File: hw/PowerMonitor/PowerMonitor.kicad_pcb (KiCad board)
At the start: 2 copper layers, 100 x 100 mm, 108 parts, among them J1 Conn_01x02_Socket, J2 Conn_01x02_Socket, J3 Conn_01x02_Socket, J4 Conn_01x02_Socket, J5 Conn_01x02_Socket, Q1 Q_PMOS_GDS, Q2 Q_PMOS_GDS, Q3 Q_PMOS_GDS, U1 TPS54202DDC, U10 LM358, U11 LM393, U12 74LVC1G32, U13 LM358, U14 LM393, U15 74LVC1G32, U2 74LVC1G32, U3 74LVC1G32, U4 NE555D, U5 LM358, U6 LM358, U7 LM358, U8 LM393, U9 74LVC1G32

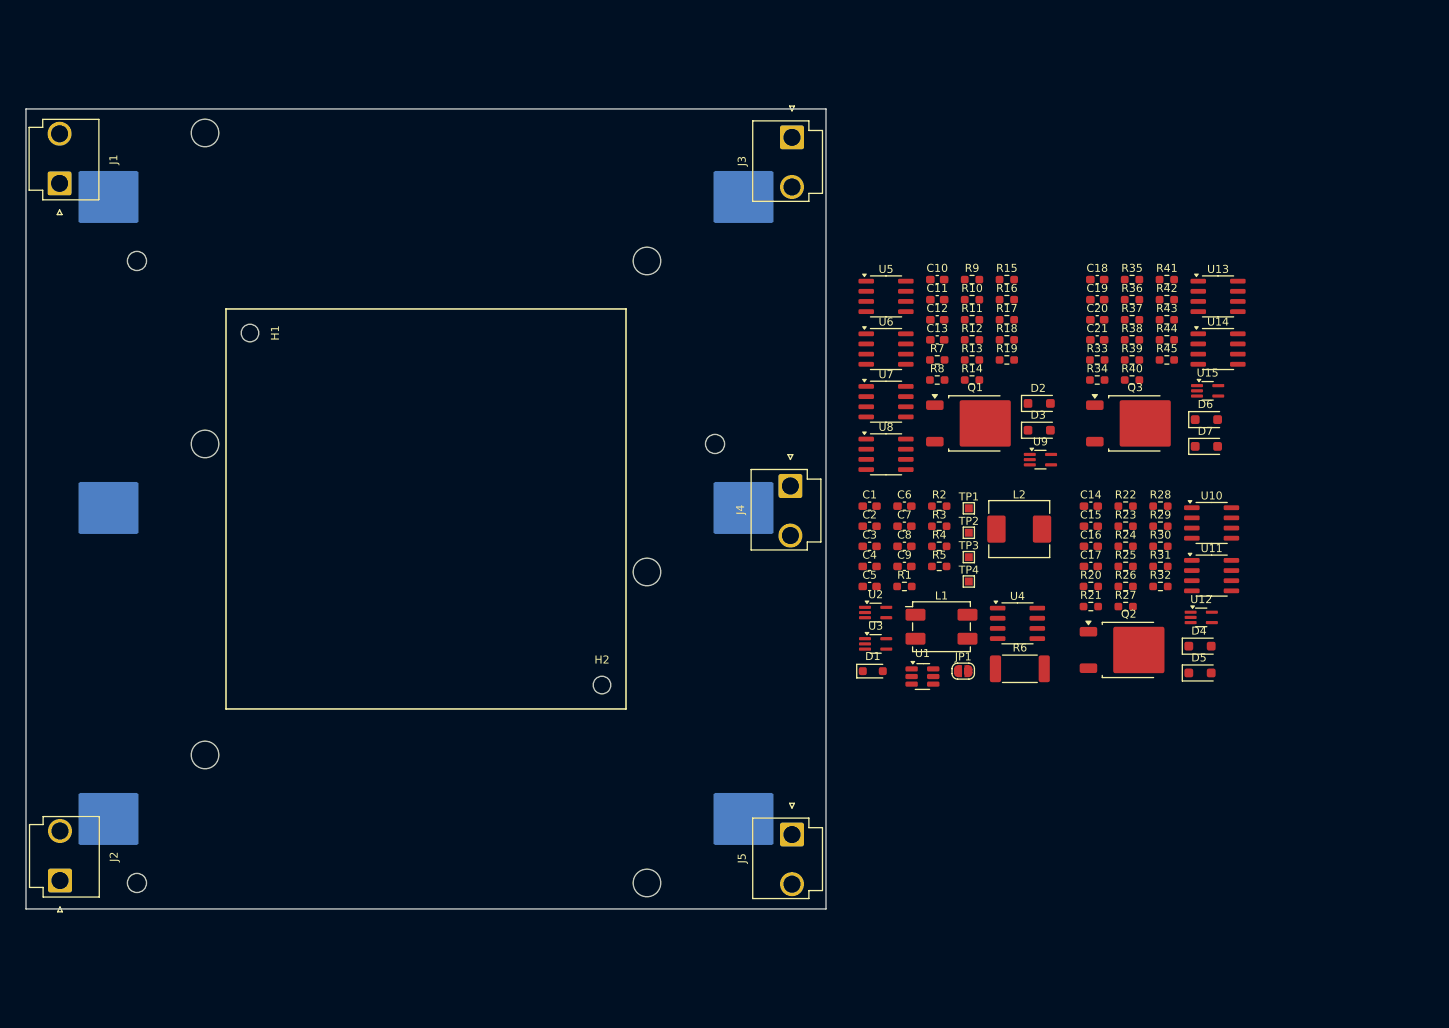
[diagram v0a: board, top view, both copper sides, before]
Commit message: ad uvov in powermon, overcurrent and prepare for latch alarm
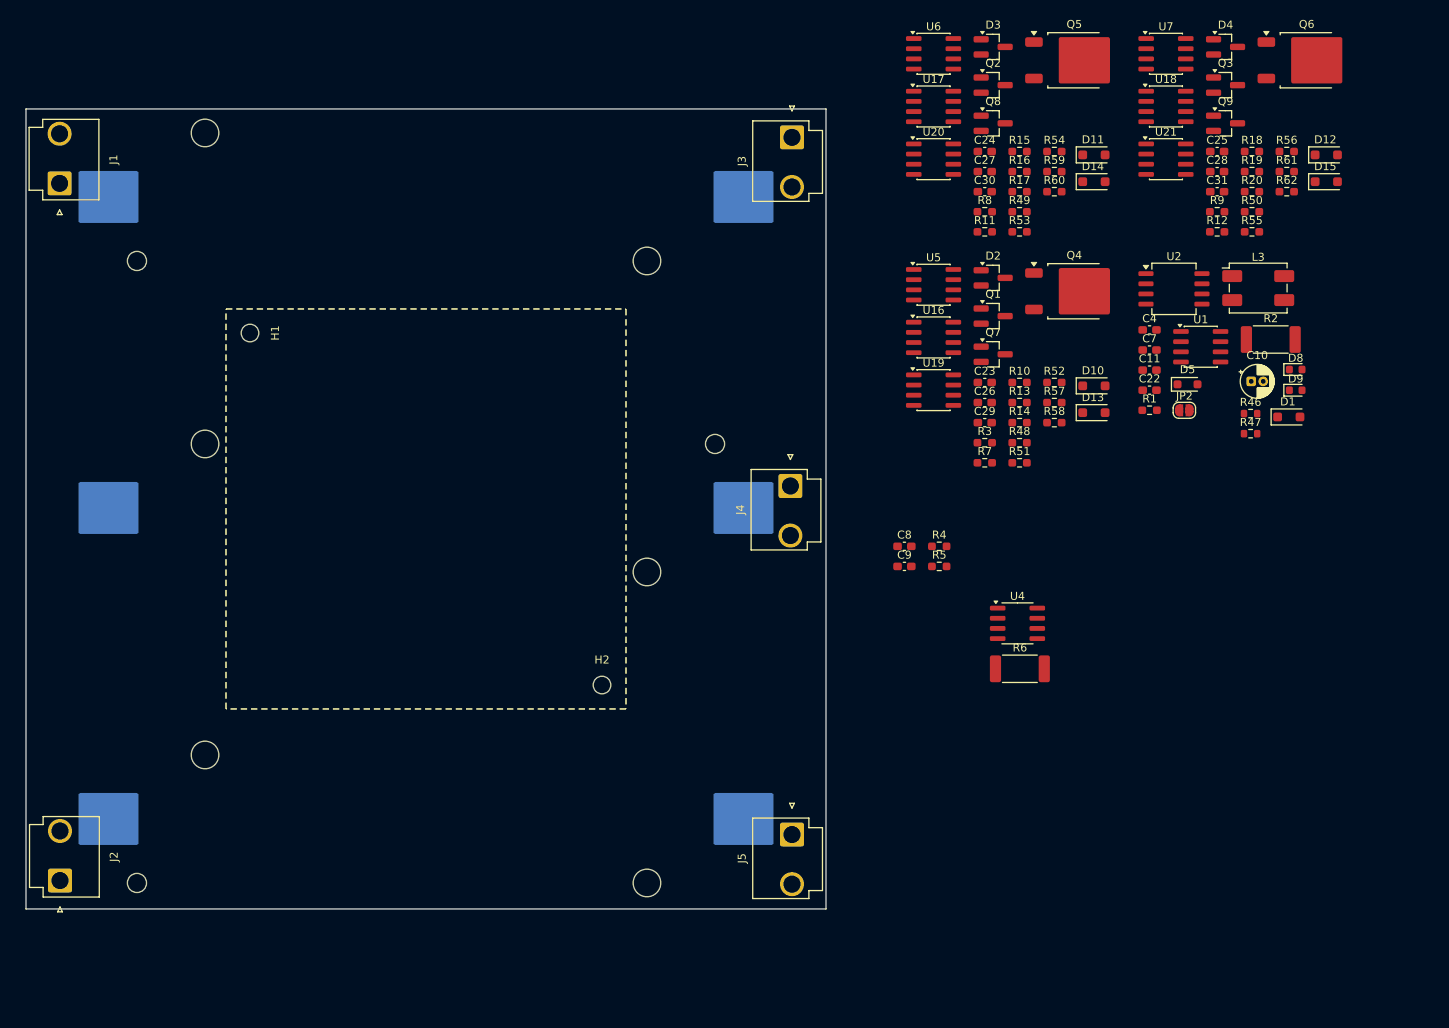
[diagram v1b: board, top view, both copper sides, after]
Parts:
- removed C1: 10 µF, Capacitor_SMD:C_0603_1608Metric_Pad1.08x0.95mm_HandSolder
- removed C12, C13, C15, C16, C17, C19, C20, C21: 1u, Capacitor_SMD:C_0603_1608Metric_Pad1.08x0.95mm_HandSolder
- removed C14, C18: 33n, Capacitor_SMD:C_0603_1608Metric_Pad1.08x0.95mm_HandSolder
- removed C2, C3: 0.1 µF, Capacitor_SMD:C_0603_1608Metric_Pad1.08x0.95mm_HandSolder
- removed C5, C6: 22 µF, Capacitor_SMD:C_0603_1608Metric_Pad1.08x0.95mm_HandSolder
- removed D6, D7: BZT52Bxx, Diode_SMD:D_SOD-123F
- removed JP1: SolderJumper_2_Open, Jumper:SolderJumper-2_P1.3mm_Open_RoundedPad1.0x1.5mm
- removed L1: L_Ferrite_Coupled_1423, Inductor_SMD:L_CommonModeChoke_TDK_ACM7060
- removed L2: KOHER_MDA7030 15uH, Inductor_SMD:L_KOHERelec_MDA7030
- removed R21, R22, R23, R24, R33, R34, R35, R36, R37: 1k, Resistor_SMD:R_0603_1608Metric_Pad0.98x0.95mm_HandSolder
- removed R25, R38: 5.6k, Resistor_SMD:R_0603_1608Metric_Pad0.98x0.95mm_HandSolder
- removed R26, R39: 1.8k, Resistor_SMD:R_0603_1608Metric_Pad0.98x0.95mm_HandSolder
- removed R27, R28, R40, R41: 150, Resistor_SMD:R_0603_1608Metric_Pad0.98x0.95mm_HandSolder
- removed R29, R42: 16k, Resistor_SMD:R_0603_1608Metric_Pad0.98x0.95mm_HandSolder
- removed R30, R43: 2k, Resistor_SMD:R_0603_1608Metric_Pad0.98x0.95mm_HandSolder
- removed R31, R32, R44, R45: 4.7k, Resistor_SMD:R_0603_1608Metric_Pad0.98x0.95mm_HandSolder
- removed TP1, TP2, TP3, TP4: TestPoint_Flag, TestPoint:TestPoint_Pad_1.0x1.0mm
- removed U10, U13: LM358, Package_SO:SOIC-8_3.9x4.9mm_P1.27mm
- removed U11, U14, U8: LM393, Package_SO:SOIC-8_3.9x4.9mm_P1.27mm
- removed U12, U15, U3, U9: 74LVC1G32, Package_TO_SOT_SMD:SOT-353_SC-70-5_Handsoldering
- added C22: 0.01 µF, Capacitor_SMD:C_0603_1608Metric_Pad1.08x0.95mm_HandSolder, F.Cu at (236.2, 75.7)
- added C23: 33n, Capacitor_SMD:C_0603_1608Metric_Pad1.08x0.95mm_HandSolder, F.Cu at (215.6, 74.7)
- added C24: 33n, Capacitor_SMD:C_0603_1608Metric_Pad1.08x0.95mm_HandSolder, F.Cu at (215.6, 45.8)
- added C25: 33n, Capacitor_SMD:C_0603_1608Metric_Pad1.08x0.95mm_HandSolder, F.Cu at (244.6, 45.8)
- added C26: 1u, Capacitor_SMD:C_0603_1608Metric_Pad1.08x0.95mm_HandSolder, F.Cu at (215.6, 77.2)
- added C27: 1u, Capacitor_SMD:C_0603_1608Metric_Pad1.08x0.95mm_HandSolder, F.Cu at (215.6, 48.3)
- added C28: 1u, Capacitor_SMD:C_0603_1608Metric_Pad1.08x0.95mm_HandSolder, F.Cu at (244.6, 48.3)
- added C29: 1u, Capacitor_SMD:C_0603_1608Metric_Pad1.08x0.95mm_HandSolder, F.Cu at (215.6, 79.7)
- added C30: 1u, Capacitor_SMD:C_0603_1608Metric_Pad1.08x0.95mm_HandSolder, F.Cu at (215.6, 50.8)
- added C31: 1u, Capacitor_SMD:C_0603_1608Metric_Pad1.08x0.95mm_HandSolder, F.Cu at (244.6, 50.8)
- added D10: BZT52Bxx, Diode_SMD:D_SOD-123F, F.Cu at (229.2, 75.1)
- added D11: BZT52Bxx, Diode_SMD:D_SOD-123F, F.Cu at (229.2, 46.2)
- added D12: BZT52Bxx, Diode_SMD:D_SOD-123F, F.Cu at (258.3, 46.2)
- added D13: BZT52Bxx, Diode_SMD:D_SOD-123F, F.Cu at (229.2, 78.5)
- added D14: BZT52Bxx, Diode_SMD:D_SOD-123F, F.Cu at (229.2, 49.6)
- added D15: BZT52Bxx, Diode_SMD:D_SOD-123F, F.Cu at (258.3, 49.6)
- added D8: RED, LED_SMD:LED_0603_1608Metric, F.Cu at (254.5, 73.1)
- added D9: GREEN, LED_SMD:LED_0603_1608Metric, F.Cu at (254.5, 75.7)
- added JP2: SolderJumper_2_Open, Jumper:SolderJumper-2_P1.3mm_Open_RoundedPad1.0x1.5mm, F.Cu at (240.5, 78.2)
- added L3: L_Ferrite_Coupled_1423, Inductor_SMD:L_CommonModeChoke_TDK_ACM7060, F.Cu at (249.8, 62.9)
- added Q4: Q_PMOS_GDS, Package_TO_SOT_SMD:TO-252-2, F.Cu at (226.8, 63.3)
- added Q5: Q_PMOS_GDS, Package_TO_SOT_SMD:TO-252-2, F.Cu at (226.8, 34.4)
- added Q6: Q_PMOS_GDS, Package_TO_SOT_SMD:TO-252-2, F.Cu at (255.8, 34.4)
- added Q7: AO3400A, Package_TO_SOT_SMD:SOT-23_Handsoldering, F.Cu at (216.6, 71.2)
- added Q8: AO3400A, Package_TO_SOT_SMD:SOT-23_Handsoldering, F.Cu at (216.6, 42.3)
- added Q9: AO3400A, Package_TO_SOT_SMD:SOT-23_Handsoldering, F.Cu at (245.7, 42.3)
- added R46: 100, Resistor_SMD:R_0603_1608Metric, F.Cu at (248.8, 78.6)
- added R47: 100, Resistor_SMD:R_0603_1608Metric, F.Cu at (248.8, 81.1)
- added R48: 1k, Resistor_SMD:R_0603_1608Metric_Pad0.98x0.95mm_HandSolder, F.Cu at (219.9, 82.2)
- added R49: 1k, Resistor_SMD:R_0603_1608Metric_Pad0.98x0.95mm_HandSolder, F.Cu at (219.9, 53.4)
- added R50: 1k, Resistor_SMD:R_0603_1608Metric_Pad0.98x0.95mm_HandSolder, F.Cu at (249.0, 53.4)
- added R51: 5.6k, Resistor_SMD:R_0603_1608Metric_Pad0.98x0.95mm_HandSolder, F.Cu at (219.9, 84.7)
- added R52: 16k, Resistor_SMD:R_0603_1608Metric_Pad0.98x0.95mm_HandSolder, F.Cu at (224.3, 74.7)
- added R53: 5.6k, Resistor_SMD:R_0603_1608Metric_Pad0.98x0.95mm_HandSolder, F.Cu at (219.9, 55.9)
- added R54: 16k, Resistor_SMD:R_0603_1608Metric_Pad0.98x0.95mm_HandSolder, F.Cu at (224.3, 45.8)
- added R55: 5.6k, Resistor_SMD:R_0603_1608Metric_Pad0.98x0.95mm_HandSolder, F.Cu at (249.0, 55.9)
- added R56: 16k, Resistor_SMD:R_0603_1608Metric_Pad0.98x0.95mm_HandSolder, F.Cu at (253.3, 45.8)
- added R57: 1.8k, Resistor_SMD:R_0603_1608Metric_Pad0.98x0.95mm_HandSolder, F.Cu at (224.3, 77.2)
- added R58: 2k, Resistor_SMD:R_0603_1608Metric_Pad0.98x0.95mm_HandSolder, F.Cu at (224.3, 79.7)
- added R59: 1.8k, Resistor_SMD:R_0603_1608Metric_Pad0.98x0.95mm_HandSolder, F.Cu at (224.3, 48.3)
- added R60: 2k, Resistor_SMD:R_0603_1608Metric_Pad0.98x0.95mm_HandSolder, F.Cu at (224.3, 50.8)
- added R61: 1.8k, Resistor_SMD:R_0603_1608Metric_Pad0.98x0.95mm_HandSolder, F.Cu at (253.3, 48.3)
- added R62: 2k, Resistor_SMD:R_0603_1608Metric_Pad0.98x0.95mm_HandSolder, F.Cu at (253.3, 50.8)
- added U16: LM358, Package_SO:SOIC-8_3.9x4.9mm_P1.27mm, F.Cu at (209.2, 69.1)
- added U17: LM358, Package_SO:SOIC-8_3.9x4.9mm_P1.27mm, F.Cu at (209.2, 40.2)
- added U18: LM358, Package_SO:SOIC-8_3.9x4.9mm_P1.27mm, F.Cu at (238.2, 40.2)
- added U19: LM393, Package_SO:SOIC-8_3.9x4.9mm_P1.27mm, F.Cu at (209.2, 75.6)
- added U20: LM393, Package_SO:SOIC-8_3.9x4.9mm_P1.27mm, F.Cu at (209.2, 46.8)
- added U21: LM393, Package_SO:SOIC-8_3.9x4.9mm_P1.27mm, F.Cu at (238.2, 46.8)
- C10: value 33n -> 470u; footprint Capacitor_SMD:C_0603_1608Metric_Pad1.08x0.95mm_HandSolder -> Capacitor_THT:CP_Radial_D4.0mm_P1.50mm
- C4, C7: value 1u -> 100n
- C9: value C -> 18 uF
- D1: value PESD15VL1BA -> BZT52Bxx; footprint Diode_SMD:D_SOD-323_HandSoldering -> Diode_SMD:D_SOD-123F
- D2, D3, D4: value BZT52Bxx -> BAT54C; footprint Diode_SMD:D_SOD-123F -> Package_TO_SOT_SMD:SOT-23_Handsoldering
- D5: value BZT52Bxx -> PESD15VL1BA; footprint Diode_SMD:D_SOD-123F -> Diode_SMD:D_SOD-323_HandSoldering
- Q1, Q2, Q3: value Q_PMOS_GDS -> AO3400A; footprint Package_TO_SOT_SMD:TO-252-2 -> Package_TO_SOT_SMD:SOT-23_Handsoldering
- R1: value 0 ohm -> 50k
- R10, R11, R7, R8, R9: value 1k -> 10k
- R12: value 5.6k -> 10k
- R13: value 1.8k -> 150
- R15: value 150 -> 0R
- R16: value 16k -> 150
- R17: value 2k -> 150
- R18: value 4.7k -> 0R
- R19: value 4.7k -> 150
- R2: value 100 kohm -> 0R001; footprint Resistor_SMD:R_0603_1608Metric_Pad0.98x0.95mm_HandSolder -> Resistor_SMD:R_2512_6332Metric_Pad1.40x3.35mm_HandSolder
- R20: value 1k -> 150
- R3: value 22 kohm -> 0R
- R5: value R -> 100k
- U1: value TPS54202DDC -> LM393; footprint Package_TO_SOT_SMD:SOT-23-6_Handsoldering -> Package_SO:SOIC-8_3.9x4.9mm_P1.27mm
- U2: value 74LVC1G32 -> INA129; footprint Package_TO_SOT_SMD:SOT-353_SC-70-5_Handsoldering -> Package_SO:SOIC-8_5.3x6.2mm_P1.27mm
- moved D4 75.0 mm to (245.7, 32.7)
- moved Q2 72.6 mm to (216.6, 37.5)
- moved D1 60.9 mm to (253.6, 79.0)
- moved U7 55.8 mm to (238.2, 33.6)
- moved U2 55.0 mm to (239.2, 63.0)
- moved U1 53.9 mm to (242.6, 70.2)
- moved R20 53.3 mm to (249.0, 50.8)
- moved D3 48.3 mm to (216.6, 32.7)
- moved R2 46.4 mm to (251.3, 69.3)
- moved C4 45.8 mm to (236.2, 68.1)
- moved Q3 43.8 mm to (245.7, 37.5)
- moved C10 41.3 mm to (248.9, 74.5)
- moved R19 38.6 mm to (249.0, 48.3)
- moved R18 38.6 mm to (249.0, 45.8)
- moved C7 37.7 mm to (236.2, 70.6)
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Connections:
- BT3 pad 2: GNDREF -> GND
- C10 pad 1: Net-(Q1-G) -> +10V
- C10 pad 2: /CellMonitor1/Vprot -> GND
- C11 pad 1: /CellMonitor1/VbatH -> GND
- C11 pad 2: GNDREF -> +10V
- C4 pad 1: +3V3 -> GND
- C4 pad 2: GNDREF -> /CellMonitor1/UVOV
- C7 pad 1: +3V3 -> GND
- C7 pad 2: GNDREF -> +10V
- C8 pad 1: +3V3 -> +10V
- C8 pad 2: GNDREF -> GND
- D1 pad 1: GNDREF -> unconnected-(D1-K-Pad1)
- D1 pad 2: +10V -> GND
- D2 pad 1: Net-(D2-K) -> /CellMonitor1/OVERVOLTAGE
- D2 pad 2: GNDREF -> /CellMonitor1/UNDERVOLTAGE
- D3 pad 1: Net-(D3-K) -> /CellMonitor2/OVERVOLTAGE
- D3 pad 2: GNDREF -> /CellMonitor2/UNDERVOLTAGE
- D4 pad 1: Net-(D4-K) -> /CellMonitor3/OVERVOLTAGE
- D4 pad 2: GNDREF -> /CellMonitor3/UNDERVOLTAGE
- D5 pad 1: Net-(D5-K) -> GND
- D5 pad 2: GNDREF -> +10V
- Q1 pad 1: Net-(Q1-G) -> /CellMonitor1/OVERVOLTAGE
- Q1 pad 2: /CellMonitor1/VbatH -> unconnected-(Q1-S-Pad2)
- Q1 pad 3: /CellMonitor1/Vprot -> unconnected-(Q1-D-Pad3)
- Q2 pad 1: Net-(Q2-G) -> /CellMonitor2/OVERVOLTAGE
- Q2 pad 2: /CellMonitor2/VbatH -> unconnected-(Q2-S-Pad2)
- Q2 pad 3: /CellMonitor2/Vprot -> unconnected-(Q2-D-Pad3)
- Q3 pad 1: Net-(Q3-G) -> /CellMonitor3/OVERVOLTAGE
- Q3 pad 2: /CellMonitor3/VbatH -> unconnected-(Q3-S-Pad2)
- Q3 pad 3: +10V -> unconnected-(Q3-D-Pad3)
- R1 pad 1: Net-(U1-VIN) -> /CellMonitor1/UVOV
- R1 pad 2: Net-(U1-EN) -> GND
- R10 pad 1: GNDREF -> /CellMonitor1/OVERVOLTAGE
- R10 pad 2: Net-(U6A--) -> GND
- R11 pad 1: Net-(R11-Pad1) -> /CellMonitor2/OVERVOLTAGE
- R11 pad 2: Net-(U6A-+) -> GND
- R12 pad 1: Net-(U8A-+) -> /CellMonitor3/OVERVOLTAGE
- R12 pad 2: Net-(R11-Pad1) -> GND
- R13 pad 1: Net-(U8B--) -> Net-(R13-Pad1)
- R13 pad 2: Net-(R11-Pad1) -> Net-(D10-K)
- R14 pad 1: Net-(R11-Pad1) -> Net-(R13-Pad1)
- R14 pad 2: Net-(D2-K) -> Net-(D13-K)
- R15 pad 1: Net-(R11-Pad1) -> Net-(R15-Pad1)
- R15 pad 2: Net-(D3-K) -> Net-(U17A--)
- R16 pad 1: GNDREF -> Net-(R15-Pad1)
- R16 pad 2: Net-(U8A-+) -> Net-(D11-K)
- R17 pad 1: GNDREF -> Net-(R15-Pad1)
- R17 pad 2: Net-(U8B--) -> Net-(D14-K)
- R18 pad 1: +3V3 -> Net-(R18-Pad1)
- R19 pad 1: +3V3 -> Net-(R18-Pad1)
- R2 pad 1: Net-(U1-FB) -> /CellMonitor3/Vprot
- R2 pad 2: +3V3 -> +10V
- R20 pad 1: Net-(Q2-G) -> Net-(R18-Pad1)
- R20 pad 2: /CellMonitor1/Vprot -> Net-(D15-K)
- R3 pad 1: Net-(U1-FB) -> Net-(R13-Pad1)
- R3 pad 2: GND -> Net-(U16A--)
- R4 pad 2: unconnected-(R4-Pad2) -> Net-(D8-A)
- R7 pad 1: Net-(Q1-G) -> /CellMonitor1/UNDERVOLTAGE
- R7 pad 2: GNDREF -> GND
- R8 pad 1: Net-(U6A-+) -> /CellMonitor2/UNDERVOLTAGE
- R8 pad 2: /CellMonitor1/Vprot -> GND
- R9 pad 1: Net-(U6A--) -> /CellMonitor3/UNDERVOLTAGE
- R9 pad 2: GNDREF -> GND
- U1 pad 1: GND -> (no net)
- U1 pad 2: Net-(U1-SW) -> (no net)
- U1 pad 3: Net-(U1-VIN) -> (no net)
- U1 pad 4: Net-(U1-FB) -> unconnected-(U1C-V--Pad4)
- U1 pad 5: Net-(U1-EN) -> (no net)
- U1 pad 6: Net-(U1-BOOT) -> (no net)
- U2 pad 1: /CellMonitor3/UVLO -> unconnected-(U2-Rg-Pad1)
- U2 pad 2: /CellMonitor2/UVLO -> unconnected-(U2---Pad2)
- U2 pad 3: GND -> unconnected-(U2-+-Pad3)
- U2 pad 4: Net-(U2-Pad4) -> unconnected-(U2-V--Pad4)
- U2 pad 5: +3V3 -> unconnected-(U2-Ref-Pad5)
- U4 pad 2: Net-(U4-TR) -> /CellMonitor1/UVOV
- U4 pad 5: unconnected-(U4-CV-Pad5) -> Net-(U4-CV)
- U4 pad 8: +3V3 -> +10V
- U5 pad 1: unconnected-(U5-Pad1) -> (no net)
- U5 pad 2: unconnected-(U5A---Pad2) -> (no net)
- U5 pad 3: unconnected-(U5A-+-Pad3) -> (no net)
- U5 pad 4: (no net) -> GND
- U5 pad 5: (no net) -> GND
- U5 pad 6: (no net) -> GND
- U5 pad 7: (no net) -> unconnected-(U5-Pad7)
- U5 pad 8: (no net) -> +10V
- U6 pad 1: Net-(R11-Pad1) -> (no net)
- U6 pad 2: Net-(U6A--) -> (no net)
- U6 pad 3: Net-(U6A-+) -> (no net)
- U6 pad 4: (no net) -> /CellMonitor1/Vprot
- U6 pad 5: (no net) -> /CellMonitor1/Vprot
- U6 pad 6: (no net) -> /CellMonitor1/Vprot
- U6 pad 7: (no net) -> unconnected-(U6-Pad7)
- U6 pad 8: (no net) -> +10V
- U7 pad 1: unconnected-(U7-Pad1) -> (no net)
- U7 pad 2: unconnected-(U7A---Pad2) -> (no net)
- U7 pad 3: unconnected-(U7A-+-Pad3) -> (no net)
- U7 pad 4: (no net) -> /CellMonitor2/Vprot
- U7 pad 5: (no net) -> /CellMonitor2/Vprot
- U7 pad 6: (no net) -> /CellMonitor2/Vprot
- U7 pad 7: (no net) -> unconnected-(U7-Pad7)
- U7 pad 8: (no net) -> +10V

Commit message: * hw/PowerMonitor/CellMonitor.kicad_sch: start PCB layout
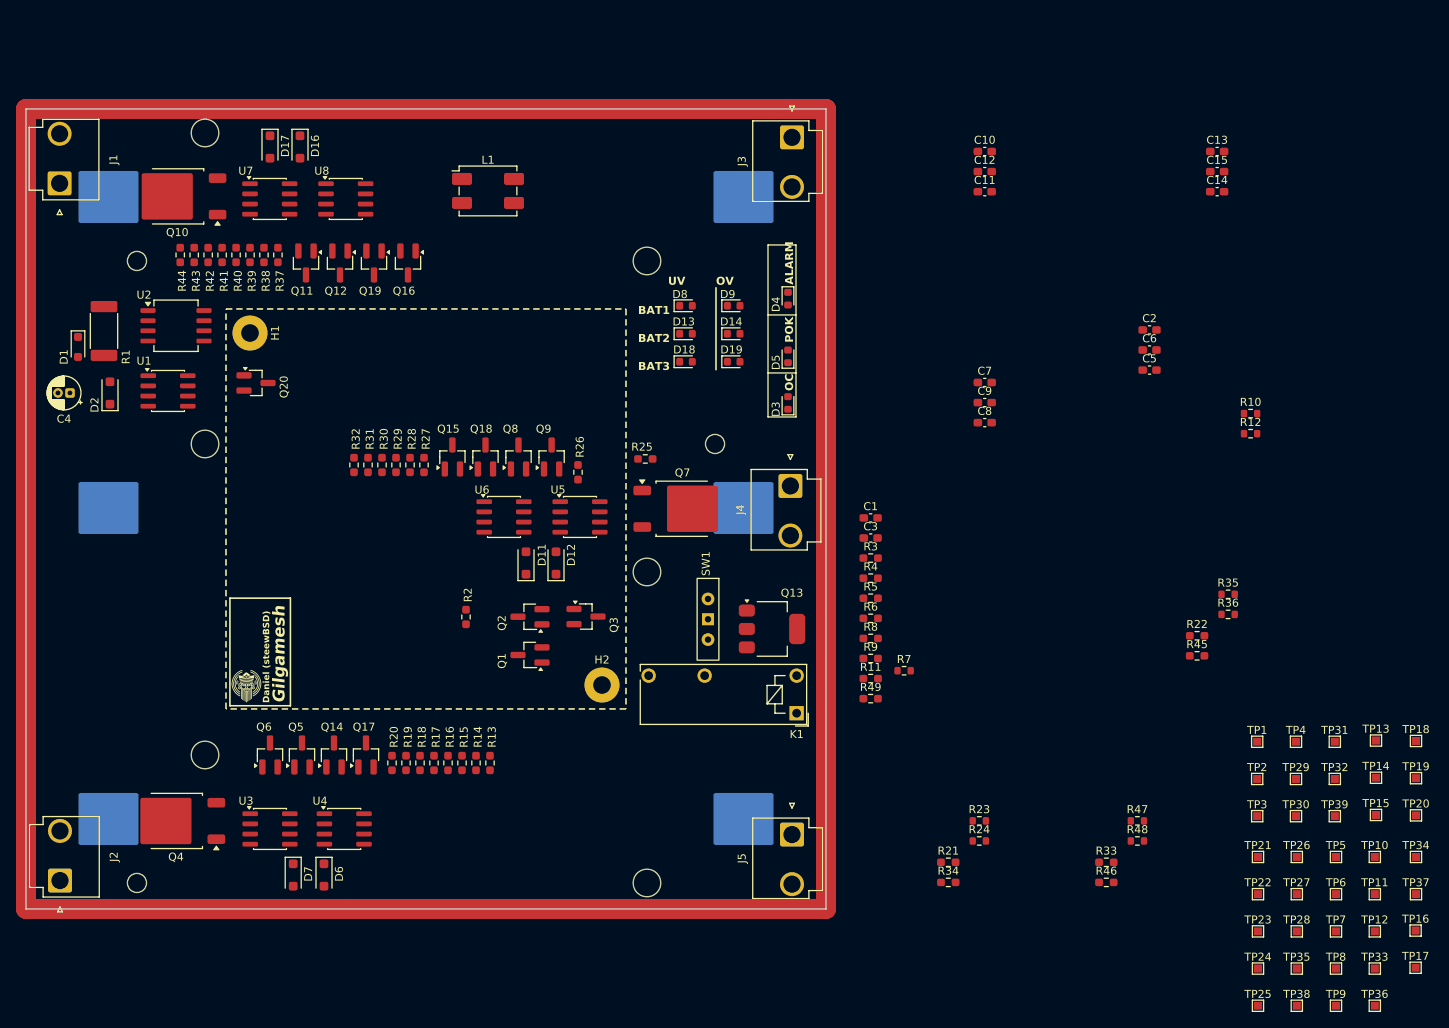
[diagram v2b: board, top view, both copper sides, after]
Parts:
- removed C22: 0.01 µF, Capacitor_SMD:C_0603_1608Metric_Pad1.08x0.95mm_HandSolder
- removed the C8 at (205.6, 95.2)
- removed the C9 at (205.6, 97.7)
- removed the D2 at (216.6, 61.6)
- removed the D4 at (245.7, 32.7)
- removed JP2: SolderJumper_2_Open, Jumper:SolderJumper-2_P1.3mm_Open_RoundedPad1.0x1.5mm
- removed the R10 at (219.9, 74.7)
- removed the R12 at (244.6, 55.9)
- removed U16, U17, U18: LM358, Package_SO:SOIC-8_3.9x4.9mm_P1.27mm
- removed U19, U20, U21: LM393, Package_SO:SOIC-8_3.9x4.9mm_P1.27mm
- added C1: 100n, Capacitor_SMD:C_0603_1608Metric_Pad1.08x0.95mm_HandSolder, F.Cu at (201.3, 91.6)
- added C3: 100n, Capacitor_SMD:C_0603_1608Metric_Pad1.08x0.95mm_HandSolder, F.Cu at (201.3, 94.1)
- added D13: RED, LED_SMD:LED_0603_1608Metric, F.Cu at (178.2, 68.6)
- added D14: RED, LED_SMD:LED_0603_1608Metric, F.Cu at (184.2, 68.6)
- added D18: RED, LED_SMD:LED_0603_1608Metric, F.Cu at (178.2, 72.1)
- added D19: RED, LED_SMD:LED_0603_1608Metric, F.Cu at (184.2, 72.1)
- added D8: RED, LED_SMD:LED_0603_1608Metric, F.Cu at (178.2, 65.1)
- added D9: RED, LED_SMD:LED_0603_1608Metric, F.Cu at (184.2, 65.1)
- added K1: Relay_SPST-NO, Relay_THT:Relay_SPST_Omron_G5NB, F.Cu at (192.1, 116.0)
- added Q1: AO3400A, Package_TO_SOT_SMD:SOT-23_Handsoldering, F.Cu at (158.8, 108.8)
- added Q13: X0202MN, Package_TO_SOT_SMD:SOT-223, F.Cu at (189.0, 105.5)
- added Q14: AO3400A, Package_TO_SOT_SMD:SOT-23_Handsoldering, F.Cu at (134.2, 121.2)
- added Q15: AO3400A, Package_TO_SOT_SMD:SOT-23_Handsoldering, F.Cu at (149.1, 84.0)
- added Q16: AO3400A, Package_TO_SOT_SMD:SOT-23_Handsoldering, F.Cu at (143.5, 59.8)
- added Q17: AO3400A, Package_TO_SOT_SMD:SOT-23_Handsoldering, F.Cu at (138.2, 121.2)
- added Q18: AO3400A, Package_TO_SOT_SMD:SOT-23_Handsoldering, F.Cu at (153.2, 84.0)
- added Q19: AO3400A, Package_TO_SOT_SMD:SOT-23_Handsoldering, F.Cu at (139.2, 59.8)
- added Q2: AO3400A, Package_TO_SOT_SMD:SOT-23_Handsoldering, F.Cu at (158.8, 104.0)
- added Q20: AO3400A, Package_TO_SOT_SMD:SOT-23_Handsoldering, F.Cu at (124.5, 74.8)
- added Q3: AO3400A, Package_TO_SOT_SMD:SOT-23_Handsoldering, F.Cu at (165.8, 104.0)
- added R21: 50k, Resistor_SMD:R_0603_1608Metric_Pad0.98x0.95mm_HandSolder, F.Cu at (211.0, 134.7)
- added R22: 50k, Resistor_SMD:R_0603_1608Metric_Pad0.98x0.95mm_HandSolder, F.Cu at (242.1, 106.3)
- added R23: 1K, Resistor_SMD:R_0603_1608Metric, F.Cu at (214.9, 129.5)
- added R24: 1K, Resistor_SMD:R_0603_1608Metric, F.Cu at (214.9, 132.0)
- added R3: 374R, Resistor_SMD:R_0603_1608Metric_Pad0.98x0.95mm_HandSolder, F.Cu at (201.3, 96.6)
- added R33: 50k, Resistor_SMD:R_0603_1608Metric_Pad0.98x0.95mm_HandSolder, F.Cu at (230.8, 134.7)
- added R34: 50k, Resistor_SMD:R_0603_1608Metric_Pad0.98x0.95mm_HandSolder, F.Cu at (211.0, 137.2)
- added R35: 1K, Resistor_SMD:R_0603_1608Metric, F.Cu at (246.0, 101.2)
- added R36: 1K, Resistor_SMD:R_0603_1608Metric, F.Cu at (246.0, 103.7)
- added R45: 50k, Resistor_SMD:R_0603_1608Metric_Pad0.98x0.95mm_HandSolder, F.Cu at (242.1, 108.9)
- added R46: 50k, Resistor_SMD:R_0603_1608Metric_Pad0.98x0.95mm_HandSolder, F.Cu at (230.8, 137.2)
- added R47: 1K, Resistor_SMD:R_0603_1608Metric, F.Cu at (234.7, 129.5)
- added R48: 1K, Resistor_SMD:R_0603_1608Metric, F.Cu at (234.7, 132.0)
- added R49: 50k, Resistor_SMD:R_0603_1608Metric_Pad0.98x0.95mm_HandSolder, F.Cu at (201.3, 114.2)
- added SW1: SW_Wuerth_450301014042, Button_Switch_THT:SW_Slide-03_Wuerth-WS-SLTV_10x2.5x6.4_P2.54mm, F.Cu at (181.0, 104.3)
- added TP1: TestPoint, TestPoint:TestPoint_Pad_1.0x1.0mm, F.Cu at (249.7, 119.6)
- added TP10: TestPoint, TestPoint:TestPoint_Pad_1.0x1.0mm, F.Cu at (264.4, 134.0)
- added TP11: TestPoint, TestPoint:TestPoint_Pad_1.0x1.0mm, F.Cu at (264.4, 138.7)
- added TP12: TestPoint, TestPoint:TestPoint_Pad_1.0x1.0mm, F.Cu at (264.4, 143.3)
- added TP13: TestPoint, TestPoint:TestPoint_Pad_1.0x1.0mm, F.Cu at (264.5, 119.5)
- added TP14: TestPoint, TestPoint:TestPoint_Pad_1.0x1.0mm, F.Cu at (264.5, 124.1)
- added TP15: TestPoint, TestPoint:TestPoint_Pad_1.0x1.0mm, F.Cu at (264.5, 128.8)
- added TP16: TestPoint, TestPoint:TestPoint_Pad_1.0x1.0mm, F.Cu at (269.4, 143.2)
- added TP17: TestPoint, TestPoint:TestPoint_Pad_1.0x1.0mm, F.Cu at (269.4, 147.8)
- added TP18: TestPoint, TestPoint:TestPoint_Pad_1.0x1.0mm, F.Cu at (269.5, 119.5)
- added TP19: TestPoint, TestPoint:TestPoint_Pad_1.0x1.0mm, F.Cu at (269.5, 124.2)
- added TP2: TestPoint, TestPoint:TestPoint_Pad_1.0x1.0mm, F.Cu at (249.7, 124.2)
- added TP20: TestPoint, TestPoint:TestPoint_Pad_1.0x1.0mm, F.Cu at (269.5, 128.8)
- added TP21: TestPoint, TestPoint:TestPoint_Pad_1.0x1.0mm, F.Cu at (249.8, 134.0)
- added TP22: TestPoint, TestPoint:TestPoint_Pad_1.0x1.0mm, F.Cu at (249.8, 138.7)
- added TP23: TestPoint, TestPoint:TestPoint_Pad_1.0x1.0mm, F.Cu at (249.8, 143.3)
- added TP24: TestPoint, TestPoint:TestPoint_Pad_1.0x1.0mm, F.Cu at (249.8, 147.9)
- added TP25: TestPoint, TestPoint:TestPoint_Pad_1.0x1.0mm, F.Cu at (249.8, 152.6)
- added TP26: TestPoint, TestPoint:TestPoint_Pad_1.0x1.0mm, F.Cu at (254.6, 134.0)
- added TP27: TestPoint, TestPoint:TestPoint_Pad_1.0x1.0mm, F.Cu at (254.6, 138.7)
- added TP28: TestPoint, TestPoint:TestPoint_Pad_1.0x1.0mm, F.Cu at (254.6, 143.3)
- added TP29: TestPoint, TestPoint:TestPoint_Pad_1.0x1.0mm, F.Cu at (254.5, 124.2)
- added TP3: TestPoint, TestPoint:TestPoint_Pad_1.0x1.0mm, F.Cu at (249.7, 128.9)
- added TP30: TestPoint, TestPoint:TestPoint_Pad_1.0x1.0mm, F.Cu at (254.5, 128.9)
- added TP31: TestPoint, TestPoint:TestPoint_Pad_1.0x1.0mm, F.Cu at (259.4, 119.6)
- added TP32: TestPoint, TestPoint:TestPoint_Pad_1.0x1.0mm, F.Cu at (259.4, 124.2)
- added TP33: TestPoint, TestPoint:TestPoint_Pad_1.0x1.0mm, F.Cu at (264.4, 147.9)
- added TP34: TestPoint, TestPoint:TestPoint_Pad_1.0x1.0mm, F.Cu at (269.5, 134.0)
- added TP35: TestPoint, TestPoint:TestPoint_Pad_1.0x1.0mm, F.Cu at (254.6, 147.9)
- added TP36: TestPoint, TestPoint:TestPoint_Pad_1.0x1.0mm, F.Cu at (264.4, 152.6)
- added TP37: TestPoint, TestPoint:TestPoint_Pad_1.0x1.0mm, F.Cu at (269.5, 138.7)
- added TP38: TestPoint, TestPoint:TestPoint_Pad_1.0x1.0mm, F.Cu at (254.6, 152.6)
- added TP39: TestPoint, TestPoint:TestPoint_Pad_1.0x1.0mm, F.Cu at (259.4, 128.9)
- added TP4: TestPoint, TestPoint:TestPoint_Pad_1.0x1.0mm, F.Cu at (254.5, 119.6)
- added TP5: TestPoint, TestPoint:TestPoint_Pad_1.0x1.0mm, F.Cu at (259.5, 134.0)
- added TP6: TestPoint, TestPoint:TestPoint_Pad_1.0x1.0mm, F.Cu at (259.5, 138.7)
- added TP7: TestPoint, TestPoint:TestPoint_Pad_1.0x1.0mm, F.Cu at (259.5, 143.3)
- added TP8: TestPoint, TestPoint:TestPoint_Pad_1.0x1.0mm, F.Cu at (259.5, 147.9)
- added TP9: TestPoint, TestPoint:TestPoint_Pad_1.0x1.0mm, F.Cu at (259.5, 152.6)
- added U3: LM358, Package_SO:SOIC-8_3.9x4.9mm_P1.27mm, F.Cu at (126.2, 130.5)
- added U8: LM393, Package_SO:SOIC-8_3.9x4.9mm_P1.27mm, F.Cu at (135.7, 51.8)
- D3: value BAT54C -> RED; footprint Package_TO_SOT_SMD:SOT-23_Handsoldering -> LED_SMD:LED_0603_1608Metric
- H1, H2: value MountingHole -> MountingHole_Pad; footprint MountingHole:MountingHole_2.2mm_M2 -> MountingHole:MountingHole_2.2mm_M2_Pad
- R11, R8: value 10k -> 50k
- R4: value R -> 50k
- R5: value 100k -> 150
- R6: value 1m -> 100R; footprint Resistor_SMD:R_2512_6332Metric_Pad1.40x3.35mm_HandSolder -> Resistor_SMD:R_0603_1608Metric_Pad0.98x0.95mm_HandSolder
- R7: value 10k -> 1K; footprint Resistor_SMD:R_0603_1608Metric_Pad0.98x0.95mm_HandSolder -> Resistor_SMD:R_0603_1608Metric
- R9: value 10k -> 0R
- U4: value NE555D -> LM393
- U6: value LM358 -> LM393
- moved C4 147.7 mm to (101.2, 76.0), turned to 180 degrees
- moved D2 147.4 mm to (106.2, 76.0), turned to 90 degrees
- moved R1 145.8 mm to (105.5, 68.2), turned to -90 degrees
- moved Q10 142.2 mm to (114.7, 51.4), turned to 180 degrees
- moved D1 138.8 mm to (102.2, 70.2), turned to -90 degrees
- moved R44 138.5 mm to (115.0, 58.8), turned to 90 degrees
- moved R43 137.2 mm to (116.8, 58.8), turned to -90 degrees
- moved D17 132.1 mm to (126.2, 45.2), turned to -90 degrees
- moved R40 131.8 mm to (122.0, 58.8), turned to 90 degrees
- moved R42 130.7 mm to (118.5, 58.8), turned to -90 degrees
- moved Q4 130.4 mm to (114.5, 129.5), turned to 180 degrees
- moved U1 129.2 mm to (113.5, 75.8)
- moved R41 129.2 mm to (120.3, 58.8), turned to -90 degrees
- moved D16 128.3 mm to (130.0, 45.2), turned to -90 degrees
- moved R39 125.3 mm to (123.8, 58.8), turned to 90 degrees
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- renumbered C24 to C10, C30 to C11, C27 to C12, C25 to C13, C31 to C14, C28 to C15, C4 to C2, C10 to C4, C11 to C5, C7 to C6, C23 to C7, C29 to C8, C26 to C9, D5 to D1, D14 to D12, D12 to D16, D15 to D17, D1 to D2, D8 to D4, D9 to D5, D10 to D6, D13 to D7, L3 to L1, Q6 to Q10, Q9 to Q11, Q3 to Q12, Q7 to Q5, Q1 to Q6, Q5 to Q7, Q2 to Q9, R2 to R1, R46 to R10, R47 to R12, R48 to R13, R3 to R14, R51 to R15, R57 to R16, R13 to R17, R14 to R18, R52 to R19, R1 to R2, R58 to R20, R49 to R25, R15 to R26, R53 to R27, R59 to R28, R16 to R29, R17 to R30, R54 to R31, R60 to R32, R50 to R37, R18 to R38, R55 to R39, R61 to R40, R19 to R41, R20 to R42, R56 to R43, R62 to R44
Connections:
- C2 pad 2: /CellMonitor1/UVOV -> /VOLT_ALARM
- D12 pad 1: Net-(D14-K) -> Net-(D12-K)
- D2 pad 1: unconnected-(D1-K-Pad1) -> Net-(D2-K)
- D3 pad 1: /CellMonitor2/OVERVOLTAGE -> Net-(D3-K)
- D3 pad 2: /CellMonitor2/UNDERVOLTAGE -> +10V
- D4 pad 2: Net-(D8-A) -> Net-(D4-A)
- D6 pad 1: Net-(D10-K) -> Net-(D6-K)
- D7 pad 1: Net-(D13-K) -> Net-(D7-K)
- J1 pad 1: VDC -> Net-(J1-Pin_1)
- J1 pad 2: GNDREF -> GND
- J2 pad 1: VDC -> Net-(J1-Pin_1)
- J2 pad 2: GNDREF -> GND
- J3 pad 1: VDC -> Net-(J1-Pin_1)
- J3 pad 2: GNDREF -> GND
- J4 pad 1: VDC -> Net-(J1-Pin_1)
- J4 pad 2: GNDREF -> GND
- J5 pad 1: VDC -> Net-(J1-Pin_1)
- J5 pad 2: GNDREF -> GND
- L1 pad 1: unconnected-(L3-Pad1) -> VDC
- L1 pad 2: unconnected-(L3-Pad2) -> GND
- L1 pad 3: unconnected-(L3-Pad3) -> GND
- L1 pad 4: unconnected-(L3-Pad4) -> Net-(J1-Pin_1)
- Q11 pad 2: unconnected-(Q9-S-Pad2) -> GND
- Q11 pad 3: unconnected-(Q9-D-Pad3) -> Net-(Q11-D)
- Q12 pad 2: unconnected-(Q3-S-Pad2) -> GND
- Q12 pad 3: unconnected-(Q3-D-Pad3) -> Net-(Q12-D)
- Q5 pad 2: unconnected-(Q7-S-Pad2) -> GND
- Q5 pad 3: unconnected-(Q7-D-Pad3) -> Net-(Q5-D)
- Q6 pad 2: unconnected-(Q1-S-Pad2) -> GND
- Q6 pad 3: unconnected-(Q1-D-Pad3) -> Net-(Q6-D)
- Q8 pad 2: unconnected-(Q8-S-Pad2) -> GND
- Q8 pad 3: unconnected-(Q8-D-Pad3) -> Net-(Q8-D)
- Q9 pad 2: unconnected-(Q2-S-Pad2) -> GND
- Q9 pad 3: unconnected-(Q2-D-Pad3) -> Net-(Q9-D)
- R11 pad 1: /CellMonitor2/OVERVOLTAGE -> +10V
- R11 pad 2: GND -> Net-(Q3-D)
- R15 pad 1: Net-(U19A--) -> Net-(U4A-+)
- R16 pad 1: Net-(U19B-+) -> Net-(U4B-+)
- R17 pad 2: Net-(D10-K) -> Net-(D6-K)
- R18 pad 2: Net-(D13-K) -> Net-(D7-K)
- R19 pad 2: Net-(U19A--) -> Net-(U4A-+)
- R2 pad 1: /CellMonitor1/UVOV -> /VOLT_ALARM
- R20 pad 2: Net-(U19B-+) -> Net-(U4B-+)
- R26 pad 1: Net-(R15-Pad1) -> Net-(R26-Pad1)
- R26 pad 2: Net-(U17A--) -> Net-(U5A--)
- R27 pad 1: Net-(U20A--) -> Net-(U6A-+)
- R27 pad 2: Net-(R15-Pad1) -> Net-(R26-Pad1)
- R28 pad 1: Net-(U20B-+) -> Net-(U6B-+)
- R28 pad 2: Net-(R15-Pad1) -> Net-(R26-Pad1)
- R29 pad 1: Net-(R15-Pad1) -> Net-(R26-Pad1)
- R30 pad 1: Net-(R15-Pad1) -> Net-(R26-Pad1)
- R30 pad 2: Net-(D14-K) -> Net-(D12-K)
- R31 pad 2: Net-(U20A--) -> Net-(U6A-+)
- R32 pad 2: Net-(U20B-+) -> Net-(U6B-+)
- R38 pad 1: Net-(R18-Pad1) -> Net-(R38-Pad1)
- R38 pad 2: Net-(U18A--) -> Net-(U7A--)
- R39 pad 2: Net-(R18-Pad1) -> Net-(R38-Pad1)
- R4 pad 1: Net-(U4-Q) -> Net-(Q1-S)
- R4 pad 2: Net-(D8-A) -> GND
- R40 pad 2: Net-(R18-Pad1) -> Net-(R38-Pad1)
- R41 pad 1: Net-(R18-Pad1) -> Net-(R38-Pad1)
- R42 pad 1: Net-(R18-Pad1) -> Net-(R38-Pad1)
- R5 pad 1: Net-(U4-DIS) -> Net-(D2-K)
- R5 pad 2: +3V3 -> +10V
- R7 pad 1: /CellMonitor1/UNDERVOLTAGE -> Net-(Q20-D)
- R7 pad 2: GND -> Net-(D3-K)
- R8 pad 1: /CellMonitor2/UNDERVOLTAGE -> /CURR_ALARM
- R9 pad 1: /CellMonitor3/UNDERVOLTAGE -> GND
- U1 pad 1: (no net) -> /CURR_ALARM
- U1 pad 2: (no net) -> Net-(D2-K)
- U1 pad 3: (no net) -> Net-(U1A-+)
- U1 pad 4: unconnected-(U1C-V--Pad4) -> GND
- U1 pad 5: (no net) -> GND
- U1 pad 6: (no net) -> GND
- U1 pad 7: (no net) -> unconnected-(U1-Pad7)
- U1 pad 8: unconnected-(U1C-V+-Pad8) -> +10V
- U2 pad 1: unconnected-(U2-Rg-Pad1) -> Net-(R3-Pad1)
- U2 pad 2: unconnected-(U2---Pad2) -> +10V
- U2 pad 3: unconnected-(U2-+-Pad3) -> /CellMonitor3/Vprot
- U2 pad 4: unconnected-(U2-V--Pad4) -> GND
- U2 pad 5: unconnected-(U2-Ref-Pad5) -> GND
- U2 pad 6: unconnected-(U2-Pad6) -> Net-(U1A-+)
- U2 pad 7: unconnected-(U2-V+-Pad7) -> +10V
- U2 pad 8: unconnected-(U2-Rg-Pad8) -> Net-(R3-Pad2)
- U4 pad 1: GND -> /CellMonitor1/UNDERVOLTAGE
- U4 pad 2: /CellMonitor1/UVOV -> Net-(D6-K)
- U4 pad 3: Net-(U4-Q) -> Net-(U4A-+)
- U4 pad 4: +3V3 -> GND
- U4 pad 5: Net-(U4-CV) -> Net-(U4B-+)
- U4 pad 6: Net-(U4-DIS) -> Net-(D7-K)
- U4 pad 7: Net-(U4-DIS) -> /CellMonitor1/OVERVOLTAGE
- U5 pad 1: (no net) -> Net-(R26-Pad1)
- U5 pad 2: (no net) -> Net-(U5A--)
- U5 pad 3: (no net) -> /CellMonitor2/Vprot
- U5 pad 4: GND -> /CellMonitor1/Vprot
- U5 pad 5: GND -> /CellMonitor1/Vprot
- U5 pad 6: GND -> /CellMonitor1/Vprot
- U6 pad 1: (no net) -> /CellMonitor2/UNDERVOLTAGE
- U6 pad 2: (no net) -> Net-(D11-K)
- U6 pad 3: (no net) -> Net-(U6A-+)
- U6 pad 4: /CellMonitor1/Vprot -> GND
- U6 pad 5: /CellMonitor1/Vprot -> Net-(U6B-+)
- U6 pad 6: /CellMonitor1/Vprot -> Net-(D12-K)
- U6 pad 7: unconnected-(U6-Pad7) -> /CellMonitor2/OVERVOLTAGE
- U7 pad 1: (no net) -> Net-(R38-Pad1)
- U7 pad 2: (no net) -> Net-(U7A--)
- U7 pad 3: (no net) -> /CellMonitor3/Vprot
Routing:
- added copper zone on In1.Cu, net +10V
- added copper zone on In2.Cu, net GND
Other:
- copper layers 2 -> 4
- board text added: "ALARM"
- board text added: "BAT1"
- board text added: "BAT2"
- board text added: "BAT3"
- board text added: "Daniel (steewBSD)"
- board text added: "Gilgamesh"
- board text added: "OC"
- board text added: "OV"
- board text added: "POK"
- board text added: "UV"
